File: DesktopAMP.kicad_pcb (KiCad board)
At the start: 2 copper layers, 100 x 100 mm, 72 parts, among them J1 Conn_02x20_Odd_Even, J2 Conn_02x01, J3 Conn_01x03, J4 Conn_01x04, J5 Conn_01x03, Q1 DMG2305UX, U1 LM1117-3.3, U2 LM2592HV, U3 LM1117-3.3, U4 DMMT5401, U5 PCM5242, U6 AT24CS01-STUM, U7 LM4780, X1 22.5792MHz, X2 24.5760MHz

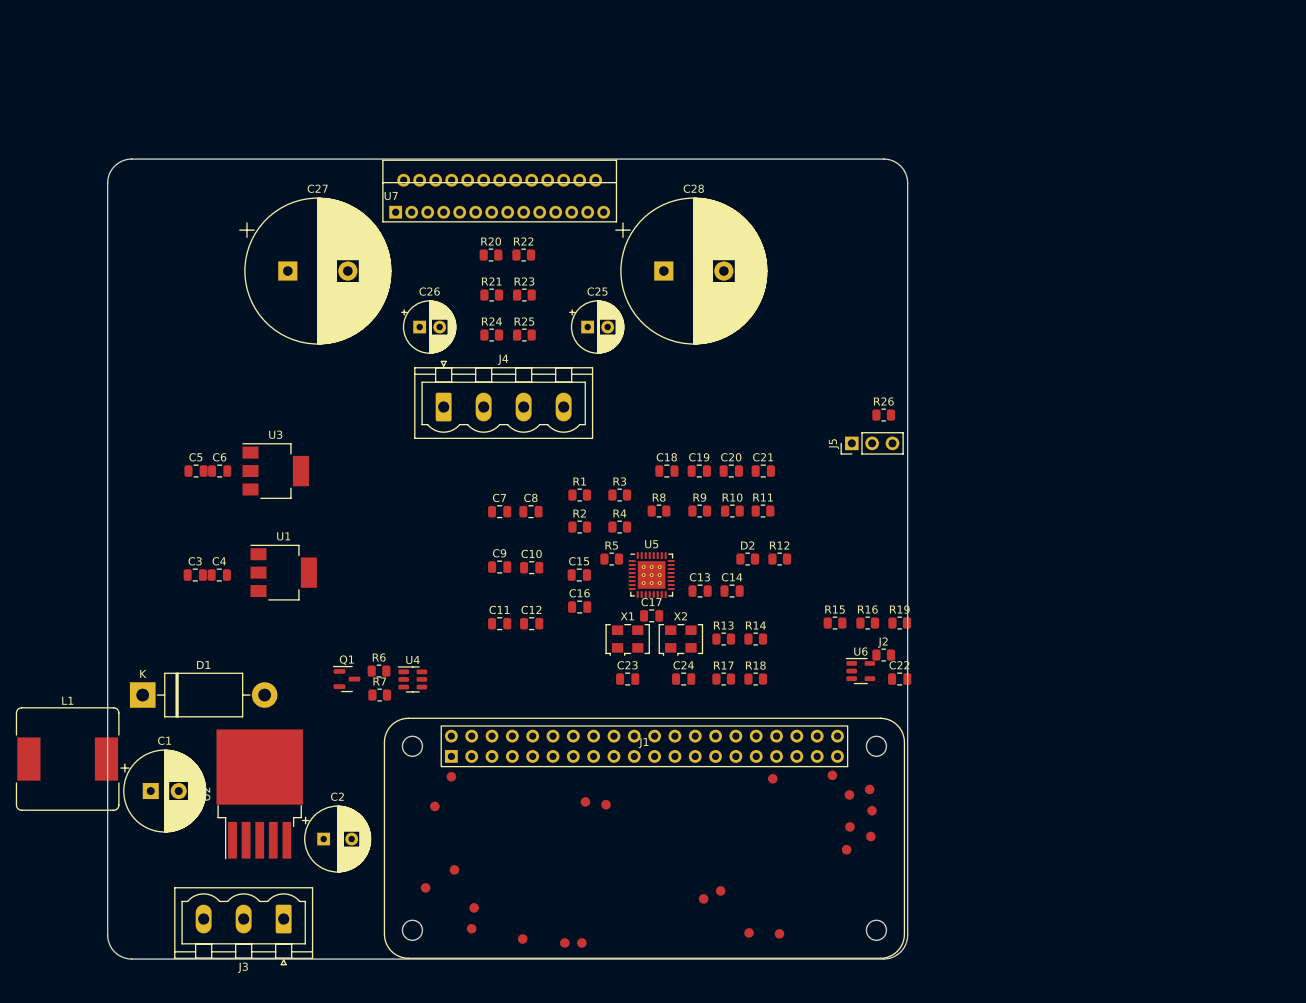
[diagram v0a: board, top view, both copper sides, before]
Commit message: Worked on placement and footprints.
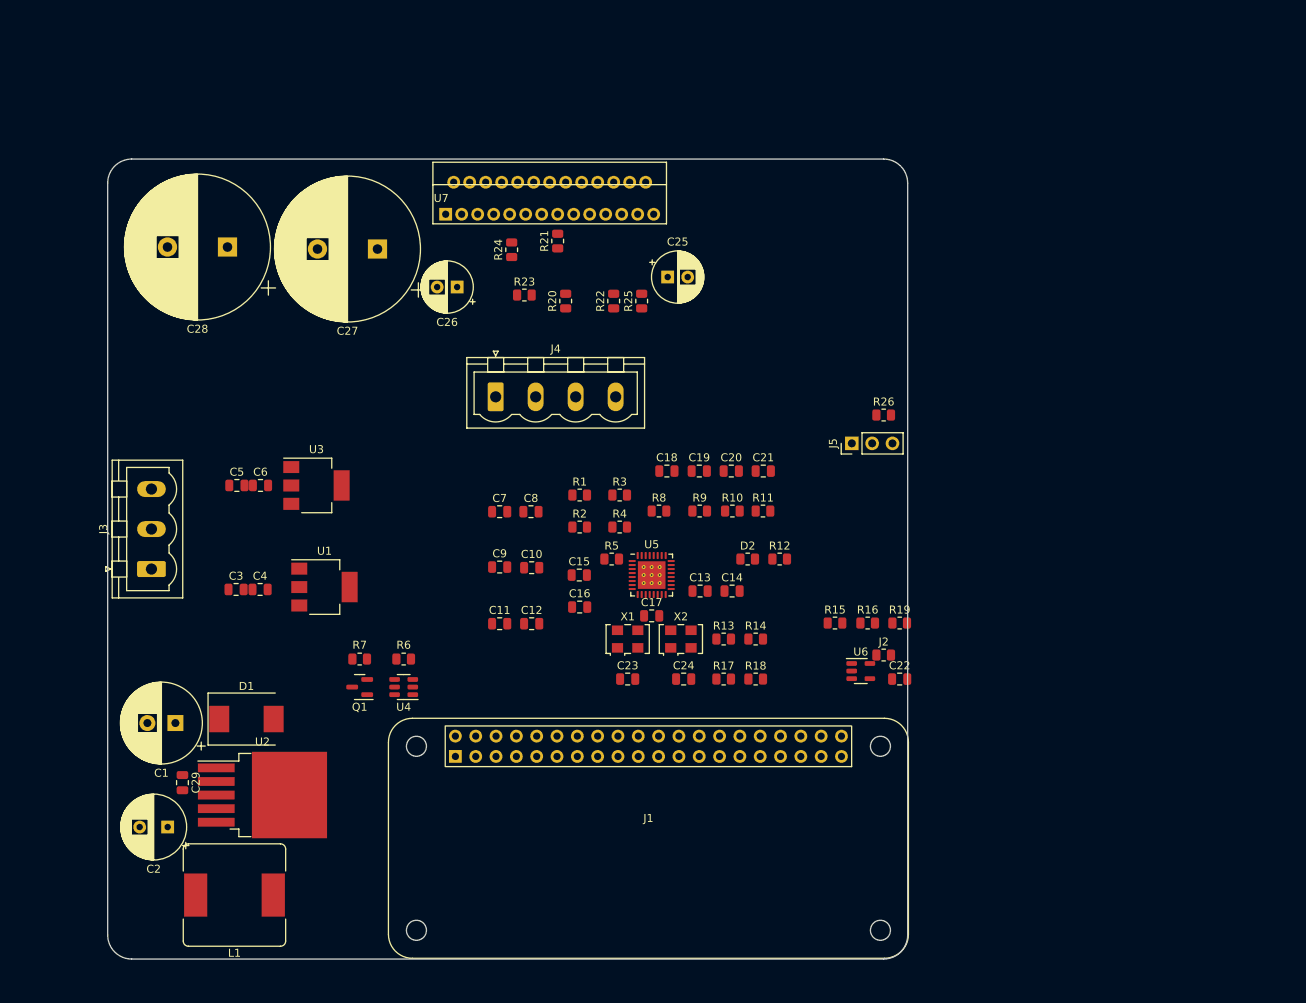
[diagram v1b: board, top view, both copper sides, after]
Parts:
- added C29: 100nF, Capacitor_SMD:C_0805_2012Metric, F.Cu at (109.3, 132.9)
- D1: value 1N5822 -> SSC54-E3/9AT; footprint Diode_THT:D_DO-201AD_P15.24mm_Horizontal -> Diode_SMD:D_SMC
- J1: footprint Etnolit:Raspberry Pi Zero 2 W -> Etnolit:RPi_Zero_2W
- moved C28 54.6 mm to (115.0, 66.0), turned to 180 degrees
- moved J3 46.8 mm to (105.5, 106.2), turned to 90 degrees
- moved L1 26.9 mm to (115.8, 147.0), turned to 180 degrees
- moved C2 19.6 mm to (107.5, 138.5), turned to 180 degrees
- moved R25 15.3 mm to (166.8, 72.8), turned to 90 degrees
- moved D1 13.3 mm to (117.3, 125.0)
- moved R22 12.6 mm to (163.2, 72.8), turned to 90 degrees
- moved C25 11.8 mm to (170.0, 69.8)
- moved C27 11.5 mm to (133.7, 66.2), turned to 180 degrees
- moved R20 11.0 mm to (157.2, 72.8), turned to 90 degrees
- moved R24 11.0 mm to (150.5, 66.3), turned to 90 degrees
- moved R21 10.7 mm to (156.2, 65.2), turned to 90 degrees
- moved C1 9.04 mm to (108.5, 125.5), turned to 180 degrees
- moved C26 6.85 mm to (143.7, 71.0), turned to 180 degrees
- moved J4 6.62 mm to (148.5, 84.7)
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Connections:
- C27 pad 2: Net-(C27-Pad2) -> GND
- C28 pad 1: Net-(C28-Pad1) -> GND
- U7 pad 10: Net-(C28-Pad1) -> VEE
- U7 pad 11: Net-(C28-Pad1) -> VEE
- U7 pad 17: Net-(C27-Pad2) -> VCC
- U7 pad 18: Net-(C28-Pad1) -> VEE
- U7 pad 2: Net-(C28-Pad1) -> VEE
- U7 pad 27: Net-(C27-Pad2) -> VCC
- U7 pad 4: Net-(C28-Pad1) -> VEE
- U7 pad 5: Net-(C27-Pad2) -> VCC
- U7 pad 8: Net-(C27-Pad2) -> VCC
- U7 pad 9: Net-(C27-Pad2) -> VCC

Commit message: Begun splitting schematic into multiple sheets.
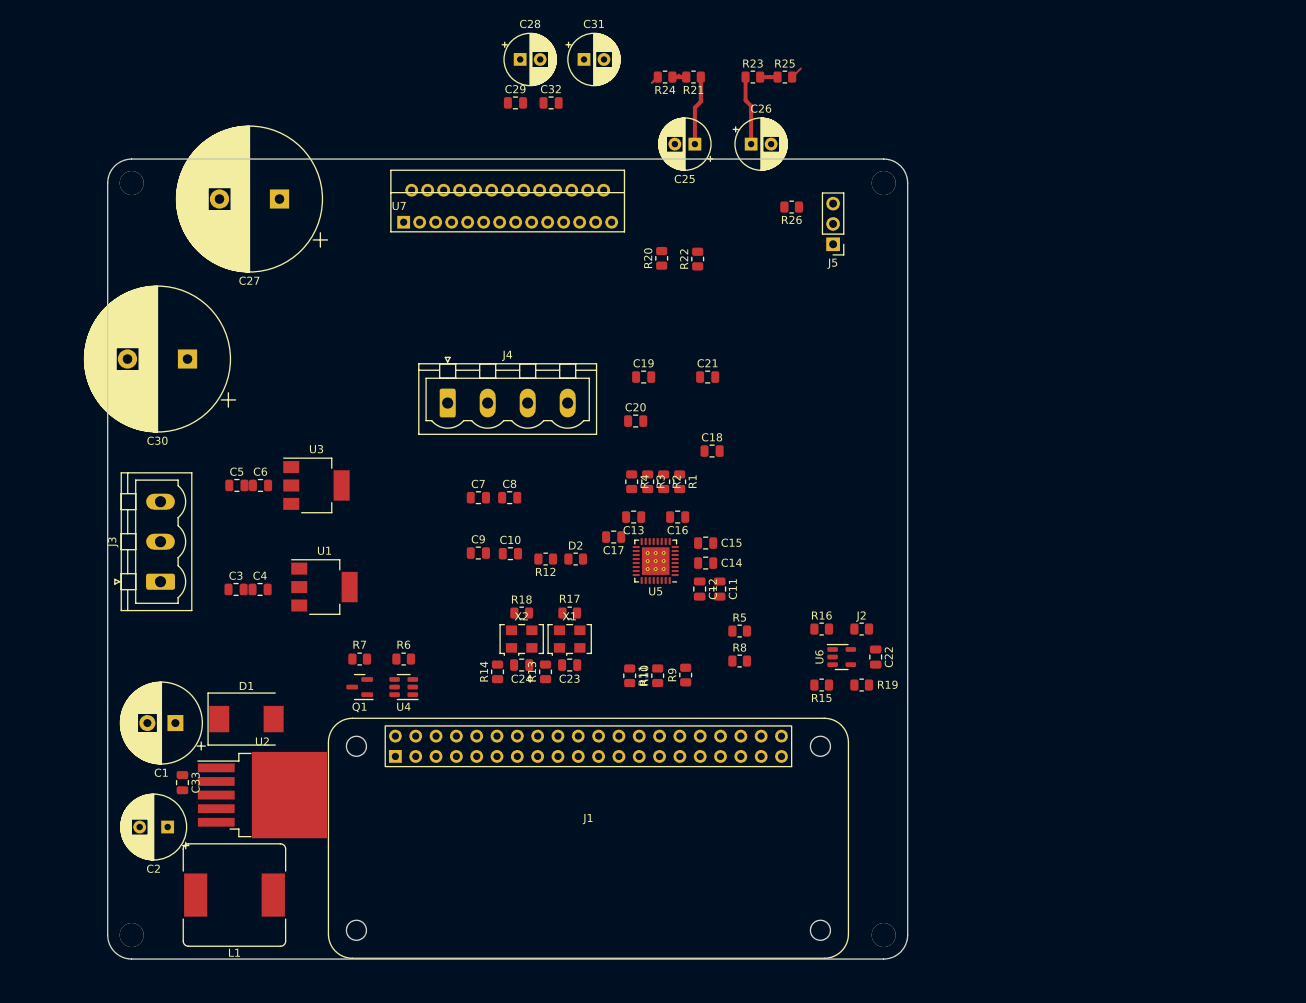
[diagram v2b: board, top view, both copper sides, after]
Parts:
- added C28: 10uF, Capacitor_THT:CP_Radial_D6.3mm_P2.50mm, F.Cu at (151.6, 42.6)
- added C29: 100nF, Capacitor_SMD:C_0805_2012Metric, F.Cu at (151.0, 48.0)
- added C31: 10uF, Capacitor_THT:CP_Radial_D6.3mm_P2.50mm, F.Cu at (159.5, 42.6)
- added C32: 100nF, Capacitor_SMD:C_0805_2012Metric, F.Cu at (155.4, 48.0)
- moved C26 40.9 mm to (180.4, 53.1), turned to 0 degrees
- moved R23 39.5 mm to (180.7, 44.8)
- moved R25 33.2 mm to (184.7, 44.8), turned to 0 degrees
- moved R14 32.5 mm to (148.7, 119.1), turned to 90 degrees
- moved R18 30.4 mm to (151.8, 111.8)
- moved R12 29.2 mm to (154.8, 105.0), turned to 180 degrees
- moved R24 28.9 mm to (169.7, 44.8), turned to 180 degrees
- moved R26 28.4 mm to (185.5, 61.0), turned to 180 degrees
- moved C11 27.8 mm to (176.5, 108.8), turned to -90 degrees
- moved R21 26.6 mm to (173.2, 44.8), turned to 180 degrees
- moved R11 26.5 mm to (165.2, 119.6), turned to -90 degrees
- moved J5 25.0 mm to (190.7, 65.7), turned to 180 degrees
- moved R13 22.6 mm to (154.7, 119.1), turned to 90 degrees
- moved R10 22.6 mm to (168.8, 119.6), turned to 90 degrees
- moved D2 21.5 mm to (158.5, 105.0)
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- renumbered C28 to C30, C29 to C33
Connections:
- net Net-(J4-Pad1) renamed /L+
- net Net-(J4-Pad4) renamed /R+
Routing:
- net Net-(C25-Pad1): track 0.00 -> 8.69 mm
- net Net-(C26-Pad1): track 0.00 -> 8.67 mm
- net Net-(R21-Pad2): track 0.00 -> 1.97 mm
- net Net-(R23-Pad2): track 0.00 -> 1.90 mm
- net /L+: track 0.00 -> 1.69 mm
- net /R+: track 0.00 -> 1.52 mm
- net (no net): vias 0 -> 4

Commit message: WIP
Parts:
- removed the J2 at (194.2, 113.8)
- added J3: Conn_02x01, Resistor_SMD:R_0805_2012Metric, F.Cu at (200.8, 91.3)
- C1: value 680uF -> 10uF; footprint Capacitor_THT:CP_Radial_D10.0mm_P3.50mm -> Capacitor_SMD:C_0805_2012Metric
- C10, C8: value 100nF -> 2.2uF
- C11, C13, C14, C4, C7: value 10uF -> 100nF
- C12: value 100nF -> 1uF
- C15: value 2.2uF -> 680uF; footprint Capacitor_SMD:C_0805_2012Metric -> Capacitor_THT:CP_Radial_D10.0mm_P3.50mm
- C16: value 2.2uF -> 100nF
- C17: value 1uF -> 10uF; footprint Capacitor_SMD:C_0805_2012Metric -> Capacitor_SMD:C_1206_3216Metric
- C18, C19, C20: footprint Capacitor_SMD:C_0805_2012Metric -> Capacitor_SMD:C_1206_3216Metric
- C2: value 220uF -> 100nF; footprint Capacitor_THT:CP_Radial_D8.0mm_P3.50mm -> Capacitor_SMD:C_0805_2012Metric
- C21: value 10uF -> 220uF; footprint Capacitor_SMD:C_0805_2012Metric -> Capacitor_THT:CP_Radial_D8.0mm_P3.50mm
- C22, C23, C24: value 100nF -> 1000pF
- C25: value 47uF -> 1000pF; footprint Capacitor_THT:CP_Radial_D6.3mm_P2.50mm -> Capacitor_SMD:C_0805_2012Metric
- C27: value 2200uF -> 47uF; footprint Capacitor_THT:CP_Radial_D18.0mm_P7.50mm -> Capacitor_THT:CP_Radial_D6.3mm_P2.50mm
- C28: value 10uF -> 2200uF; footprint Capacitor_THT:CP_Radial_D6.3mm_P2.50mm -> Capacitor_THT:CP_Radial_D18.0mm_P7.50mm
- C29: value 100nF -> 2200uF; footprint Capacitor_SMD:C_0805_2012Metric -> Capacitor_THT:CP_Radial_D18.0mm_P7.50mm
- C3: value 10uF -> 2.2uF
- C30: value 2200uF -> 10uF; footprint Capacitor_THT:CP_Radial_D18.0mm_P7.50mm -> Capacitor_THT:CP_Radial_D6.3mm_P2.50mm
- C9: value 2.2uF -> 10uF
- D1: value SSC54-E3/9AT -> LED; footprint Diode_SMD:D_SMC -> Resistor_SMD:R_0805_2012Metric
- D2: value LED -> SSC54-E3/9AT; footprint Resistor_SMD:R_0805_2012Metric -> Diode_SMD:D_SMC
- R1, R4: value 470R -> 10K
- R10, R11: value 100R -> 10K
- R12: value 3K9 -> 100R
- R13, R6, R8: value 10K -> 100R
- R15: value 3K9 -> 47K
- R16: value 3K9 -> 470R
- R17, R18: value 100R -> 470R
- R19: value 1K -> 470R
- R2, R3: value 470R -> 3K9
- R20, R22: value 470R -> 1K
- R5: value 10K -> 1K
- R7: value 47K -> 100R
- R9: value 100R -> 3K9
- U1: value LM1117-3.3 -> AT24CS01-STUM; footprint Package_TO_SOT_SMD:SOT-223-3_TabPin2 -> Package_TO_SOT_SMD:SOT-23-5
- U2: value LM2592HV -> PCM5242; footprint Package_TO_SOT_SMD:TO-263-5_TabPin3 -> Package_DFN_QFN:Texas_S-PVQFN-N32_EP3.45x3.45mm_ThermalVias
- U3: value LM1117-3.3 -> LM2592HV; footprint Package_TO_SOT_SMD:SOT-223-3_TabPin2 -> Package_TO_SOT_SMD:TO-263-5_TabPin3
- U4: value DMMT5401 -> LM1117-3.3; footprint Package_TO_SOT_SMD:SOT-23-6 -> Package_TO_SOT_SMD:SOT-223-3_TabPin2
- U5: value PCM5242 -> LM1117-3.3; footprint Package_DFN_QFN:Texas_S-PVQFN-N32_EP3.45x3.45mm_ThermalVias -> Package_TO_SOT_SMD:SOT-223-3_TabPin2
- U6: value AT24CS01-STUM -> DMMT5401; footprint Package_TO_SOT_SMD:SOT-23-5 -> Package_TO_SOT_SMD:SOT-23-6
- moved Q1 116.1 mm to (246.1, 102.5), turned to 0 degrees
- moved C3 115.0 mm to (223.7, 68.5)
- moved C1 110.8 mm to (207.5, 75.8), turned to 0 degrees
- moved C2 106.0 mm to (200.8, 88.3), turned to 0 degrees
- moved U2 104.7 mm to (202.3, 70.6)
- moved C6 103.1 mm to (219.2, 71.5)
- moved C5 102.5 mm to (216.4, 74.5)
- moved D1 101.1 mm to (209.7, 83.8)
- moved U4 97.5 mm to (233.1, 104.4), turned to 0 degrees
- moved L1 93.9 mm to (205.7, 119.6), turned to 0 degrees
- moved R7 93.8 mm to (216.4, 77.5), turned to 0 degrees
- moved R6 92.9 mm to (220.8, 77.5)
- moved C4 91.3 mm to (206.0, 80.9)
- moved R14 86.5 mm to (234.8, 110.0), turned to 0 degrees
- moved U3 82.1 mm to (207.5, 106.4)
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- renumbered J3 to J2
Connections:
- net /L+ renamed /Analog/L+
- net /MUTE renamed /Analog/MUTE
- net /R+ renamed /Analog/R+
- C1 pad 1: VCC -> DVDD
- C10 pad 1: /AVDD -> Net-(C10-Pad1)
- C10 pad 2: GND -> Net-(C10-Pad2)
- C11 pad 1: Net-(C11-Pad1) -> GND
- C11 pad 2: GND -> DVDD
- C12 pad 1: Net-(C11-Pad1) -> Net-(C12-Pad1)
- C13 pad 1: /AVDD -> GND
- C13 pad 2: GND -> DVDD
- C14 pad 1: /AVDD -> GND
- C14 pad 2: GND -> DVDD
- C15 pad 1: Net-(C15-Pad1) -> VCC
- C15 pad 2: Net-(C15-Pad2) -> GND
- C16 pad 1: GND -> VCC
- C16 pad 2: Net-(C16-Pad2) -> GND
- C17 pad 1: Net-(C17-Pad1) -> /Power/5V
- C18 pad 1: /OUTL+ -> /Power/5V
- C19 pad 1: GND -> DVDD
- C2 pad 1: /5V -> DVDD
- C20 pad 1: GND -> AVDD
- C21 pad 1: /OUTR+ -> /Power/5V
- C22 pad 2: /DVDD -> Net-(C22-Pad2)
- C23 pad 2: /DVDD -> Net-(C23-Pad2)
- C24 pad 2: /DVDD -> Net-(C24-Pad2)
- C27 pad 1: VCC -> Net-(C27-Pad1)
- C29 pad 1: VCC -> GND
- C29 pad 2: GND -> VEE
- C3 pad 1: /5V -> AVDD
- C30 pad 1: GND -> VCC
- C30 pad 2: VEE -> GND
- C32 pad 1: VEE -> VCC
- C33 pad 1: VCC -> VEE
- C4 pad 1: /DVDD -> AVDD
- C5 pad 1: /5V -> Net-(C5-Pad1)
- C6 pad 1: /AVDD -> AVDD
- C7 pad 1: /DVDD -> Net-(C5-Pad1)
- C8 pad 1: /DVDD -> GND
- C8 pad 2: GND -> Net-(C8-Pad2)
- C9 pad 1: /AVDD -> AVDD
- D1 pad 2: GND -> Net-(D1-Pad2)
- D2 pad 2: Net-(D2-Pad2) -> GND
- J1 pad 12: BCK -> /Digital/BCK
- J1 pad 2: /5VBK -> /Power/5VBK
- J1 pad 27: ID_SD -> /Digital/ID_SC
- J1 pad 28: ID_SC -> /Digital/ID_SD
- J1 pad 3: SDA -> /Digital/SDA
- J1 pad 35: LRCK -> /Digital/LRCK
- J1 pad 4: /5VBK -> /Power/5VBK
- J1 pad 40: DIN -> /Digital/DIN
- J1 pad 5: SCL -> /Digital/SCL
- L1 pad 1: Net-(D1-Pad1) -> Net-(D2-Pad1)
- L1 pad 2: /5V -> /Power/5V
- Q1 pad 2: /5VBK -> /Power/5VBK
- Q1 pad 3: /5V -> /Power/5V
- R1 pad 1: /OUTL+ -> Net-(R1-Pad1)
- R1 pad 2: Net-(R1-Pad2) -> DVDD
- R10 pad 1: DIN -> GND
- R10 pad 2: Net-(R10-Pad2) -> /Digital/GPIO6
- R11 pad 1: Net-(R11-Pad1) -> GND
- R11 pad 2: BCK -> /Digital/GPIO3
- R12 pad 1: Net-(D2-Pad1) -> Net-(R12-Pad1)
- R12 pad 2: GND -> /Digital/CLK
- R13 pad 1: GND -> Net-(R13-Pad1)
- R13 pad 2: /GPIO6 -> /Digital/CLK
- R14 pad 1: GND -> Net-(R14-Pad1)
- R14 pad 2: /GPIO3 -> GND
- R15 pad 1: ID_SD -> Net-(Q1-Pad1)
- R15 pad 2: /DVDD -> GND
- R16 pad 1: /DVDD -> Net-(C22-Pad2)
- R16 pad 2: ID_SC -> /Analog/OUTL+
- R17 pad 1: Net-(R17-Pad1) -> Net-(C23-Pad2)
- R17 pad 2: /CLK -> /Analog/OUTL-
- R18 pad 1: Net-(R18-Pad1) -> Net-(C25-Pad1)
- R18 pad 2: /CLK -> /Analog/OUTR+
- R19 pad 1: Net-(J2-Pad1) -> Net-(C24-Pad2)
- R19 pad 2: /DVDD -> /Analog/OUTR-
- R2 pad 1: GND -> /Digital/ID_SD
- R2 pad 2: Net-(R2-Pad2) -> DVDD
- R20 pad 1: /OUTL+ -> Net-(C22-Pad2)
- R22 pad 1: /OUTR+ -> Net-(C26-Pad1)
- R23 pad 1: Net-(C26-Pad1) -> Net-(C27-Pad1)
- R24 pad 1: Net-(R21-Pad2) -> Net-(R22-Pad2)
- R3 pad 1: GND -> DVDD
- R3 pad 2: Net-(R3-Pad2) -> /Digital/ID_SC
- R4 pad 1: /OUTR+ -> Net-(R4-Pad1)
- R4 pad 2: Net-(R4-Pad2) -> DVDD
- R5 pad 1: Net-(R5-Pad1) -> Net-(J3-Pad1)
- R5 pad 2: /DVDD -> DVDD
- R6 pad 1: Net-(R6-Pad1) -> /Digital/LRCK
- R6 pad 2: GND -> Net-(R6-Pad2)
- R7 pad 1: Net-(Q1-Pad1) -> /Digital/DIN
- R7 pad 2: GND -> Net-(R7-Pad2)
- R8 pad 2: /DVDD -> /Digital/BCK
- R9 pad 1: LRCK -> Net-(D1-Pad1)
- R9 pad 2: Net-(R9-Pad2) -> GND
- U1 pad 1: GND -> /Digital/ID_SC
- U1 pad 2: /DVDD -> GND
- U1 pad 3: /5V -> /Digital/ID_SD
- U2 pad 1: VCC -> Net-(R1-Pad1)
- U2 pad 2: Net-(D1-Pad1) -> Net-(C5-Pad1)
- U2 pad 4: /5V -> DVDD
- U2 pad 5: GND -> AVDD
- U3 pad 1: GND -> VCC
- U3 pad 2: /AVDD -> Net-(D2-Pad1)
- U3 pad 3: /5V -> GND
- U4 pad 1: Net-(R6-Pad1) -> GND
- U4 pad 2: Net-(R6-Pad1) -> DVDD
- U4 pad 3: Net-(R6-Pad1) -> /Power/5V
- U5 pad 1: Net-(R5-Pad1) -> GND
- U5 pad 2: Net-(C11-Pad1) -> AVDD
- U5 pad 3: GND -> /Power/5V
- U6 pad 1: ID_SC -> Net-(R14-Pad1)
- U6 pad 2: GND -> Net-(R14-Pad1)
- U6 pad 3: ID_SD -> Net-(R14-Pad1)
- U6 pad 4: /DVDD -> Net-(Q1-Pad1)
- U6 pad 5: Net-(J2-Pad1) -> /Power/5VBK
- U7 pad 15: Net-(R21-Pad2) -> Net-(R22-Pad2)
- U7 pad 22: Net-(R22-Pad2) -> Net-(R21-Pad2)
- X1 pad 1: /GPIO6 -> /Digital/GPIO6
- X1 pad 3: Net-(R17-Pad1) -> Net-(R12-Pad1)
- X1 pad 4: /DVDD -> DVDD
- X2 pad 1: /GPIO3 -> /Digital/GPIO3
- X2 pad 3: Net-(R18-Pad1) -> Net-(R13-Pad1)
- X2 pad 4: /DVDD -> DVDD
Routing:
- net Net-(C25-Pad1): track 8.69 -> 0.00 mm
- net Net-(C26-Pad1): track 8.67 -> 0.00 mm
- net Net-(R21-Pad2): track 1.97 -> 0.00 mm
- net Net-(R23-Pad2): track 1.90 -> 0.00 mm
- net /Analog/L+: track 1.69 -> 0.00 mm
- net /Analog/R+: track 1.52 -> 0.00 mm

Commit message: WIP
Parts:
- removed the C22 at (142.5, 70.1)
- removed the C26 at (131.7, 80.6)
- removed the C27 at (123.7, 88.4)
- removed the J4 at (153.0, 100.5)
- removed R4: 10K, Resistor_SMD:R_0805_2012Metric
- added C23: 2.2nF, Capacitor_SMD:C_0805_2012Metric, F.Cu at (184.8, 83.9)
- added C32: 100uF, Capacitor_THT:CP_Radial_D6.3mm_P2.50mm, F.Cu at (158.3, 92.1)
- added C33: 10uF, Capacitor_THT:CP_Radial_D6.3mm_P2.50mm, F.Cu at (182.1, 56.5)
- added C34: 100nF, Capacitor_THT:C_Rect_L7.2mm_W2.5mm_P5.00mm_FKS2_FKP2_MKS2_MKP2, F.Cu at (176.8, 56.7)
- added D3: ZF16V, Diode_SMD:D_0805_2012Metric, F.Cu at (162.9, 96.2)
- added J3: Conn_01x04, Connector_Phoenix_MSTB:PhoenixContact_MSTBVA_2,5_4-G_1x04_P5.00mm_Vertical, F.Cu at (106.0, 85.0)
- added R26: 20K, Resistor_SMD:R_0805_2012Metric, F.Cu at (167.9, 59.4)
- added R27: 20K, Resistor_SMD:R_0805_2012Metric, F.Cu at (187.4, 55.3)
- added R28: 3R16, 1W, Resistor_THT:R_Axial_DIN0309_L9.0mm_D3.2mm_P12.70mm_Horizontal, F.Cu at (112.5, 62.3)
- added R29: 3R16, 1W, Resistor_THT:R_Axial_DIN0309_L9.0mm_D3.2mm_P12.70mm_Horizontal, F.Cu at (112.5, 92.7)
- C11, C13, C14, C16, C2, C4, C7: footprint Capacitor_SMD:C_0805_2012Metric -> Capacitor_SMD:C_0603_1608Metric
- C22: renamed from C23; value 1000pF -> 2.2nF
- C24, C25: value 1000pF -> 100nF; footprint Capacitor_SMD:C_0805_2012Metric -> Capacitor_THT:C_Rect_L7.2mm_W2.5mm_P5.00mm_FKS2_FKP2_MKS2_MKP2
- C30: renamed from C32; footprint Capacitor_SMD:C_0805_2012Metric -> Capacitor_THT:C_Rect_L7.2mm_W2.5mm_P5.00mm_FKS2_FKP2_MKS2_MKP2
- C31: renamed from C33; footprint Capacitor_SMD:C_0805_2012Metric -> Capacitor_THT:C_Rect_L7.2mm_W2.5mm_P5.00mm_FKS2_FKP2_MKS2_MKP2
- C9: value 10uF -> 100nF; footprint Capacitor_SMD:C_0805_2012Metric -> Capacitor_SMD:C_0603_1608Metric
- D1: footprint Resistor_SMD:R_0805_2012Metric -> LED_SMD:LED_0805_2012Metric
- J1: footprint Etnolit:RPi_Zero_2W -> Etnolit:RPi_Zero_2W_SMD
- J4: renamed from J3; footprint Resistor_SMD:R_0805_2012Metric -> Connector_PinHeader_2.54mm:PinHeader_1x02_P2.54mm_Vertical
- R21, R22: footprint Resistor_SMD:R_0805_2012Metric -> Resistor_THT:R_Axial_DIN0207_L6.3mm_D2.5mm_P7.62mm_Horizontal
- moved C21 118.7 mm to (108.0, 115.3)
- moved C16 108.7 mm to (121.7, 113.0), turned to 180 degrees
- moved Q1 107.5 mm to (142.3, 130.6), turned to 180 degrees
- moved C15 95.2 mm to (125.5, 109.4), turned to 90 degrees
- moved C17 93.7 mm to (153.7, 136.3), turned to 90 degrees
- moved R14 91.8 mm to (146.8, 136.3), turned to 90 degrees
- moved R15 90.4 mm to (146.8, 130.6), turned to 90 degrees
- moved D2 89.3 mm to (129.0, 122.9), turned to -90 degrees
- moved U3 88.9 mm to (120.0, 122.5), turned to -90 degrees
- moved L1 87.4 mm to (120.1, 137.7), turned to 180 degrees
- moved U6 83.8 mm to (142.3, 136.3), turned to 90 degrees
- moved U4 78.8 mm to (160.5, 135.2)
- moved C22 70.4 mm to (188.8, 83.9)
- moved C18 69.9 mm to (178.2, 136.3), turned to 90 degrees
- moved C11 66.1 mm to (164.5, 111.4)
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- renumbered C28 to C26, C29 to C27, C30 to C28, C31 to C29, R26 to R30
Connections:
- C22 pad 1: GND -> Net-(C22-Pad1)
- C22 pad 2: Net-(C23-Pad2) -> Net-(C22-Pad2)
- J5 pad 3: Net-(J5-Pad3) -> Net-(D3-Pad1)
- R17 pad 1: Net-(C23-Pad2) -> Net-(C22-Pad1)
- R18 pad 1: Net-(C25-Pad1) -> Net-(C23-Pad2)
- R18 pad 2: /Analog/OUTR+ -> /Analog/OUTR-
- R19 pad 1: Net-(C24-Pad2) -> Net-(C23-Pad1)
- R19 pad 2: /Analog/OUTR- -> /Analog/OUTR+
- R21 pad 1: Net-(C25-Pad1) -> Net-(C22-Pad1)
- R22 pad 1: Net-(C26-Pad1) -> Net-(C23-Pad2)
- R23 pad 1: Net-(C27-Pad1) -> Net-(C23-Pad1)
- R24 pad 1: Net-(R22-Pad2) -> Net-(R20-Pad2)
- R24 pad 2: /Analog/L+ -> GND
- R25 pad 1: Net-(R23-Pad2) -> Net-(R21-Pad2)
- R25 pad 2: /Analog/R+ -> /Analog/L_{out}+
- R30 pad 1: Net-(J5-Pad3) -> Net-(C32-Pad1)
- U2 pad 24: Net-(R4-Pad1) -> Net-(R1-Pad1)
- U2 pad 32: Net-(R4-Pad1) -> Net-(R1-Pad1)
- U7 pad 15: Net-(R22-Pad2) -> Net-(R21-Pad2)
- U7 pad 21: Net-(R23-Pad2) -> Net-(R22-Pad2)
- U7 pad 22: Net-(R21-Pad2) -> Net-(R23-Pad2)
- U7 pad 25: /Analog/R+ -> /Analog/R_{out}+
- U7 pad 7: /Analog/L+ -> /Analog/L_{out}+
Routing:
- net GND: track 0.00 -> 614.6 mm, vias 0 -> 68
- net VCC: track 0.00 -> 160.7 mm
- net /Power/5V: track 0.00 -> 121.5 mm
- net DVDD: track 0.00 -> 121.1 mm, vias 0 -> 10
- net VEE: track 0.00 -> 112.5 mm
- net /Analog/R_{out}+: track 0.00 -> 79.4 mm
- net AVDD: track 0.00 -> 76.8 mm, vias 0 -> 10
- net /Analog/L_{out}+: track 0.00 -> 60.1 mm
- net /Digital/SDA: track 0.00 -> 57.3 mm
- net /Digital/SCL: track 0.00 -> 52.2 mm
- net /Digital/BCK: track 0.00 -> 34.5 mm
- net Net-(D2-Pad1): track 0.00 -> 33.1 mm
- net Net-(R20-Pad2): track 0.00 -> 31.2 mm
- net Net-(C22-Pad1): track 0.00 -> 23.4 mm
- net /Digital/LRCK: track 0.00 -> 22.8 mm
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- added copper zone on B.Cu, net AVDD
- added copper zone on F.Cu, net AVDD
- added copper zone on B.Cu, net DVDD
- added copper zone on F.Cu, net DVDD
- added copper zone on B.Cu, net GND
